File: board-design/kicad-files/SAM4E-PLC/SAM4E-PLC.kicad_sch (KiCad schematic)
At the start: 16 parts, among them U1 MCP7940N-xSN, U2 ATSAM4E16E

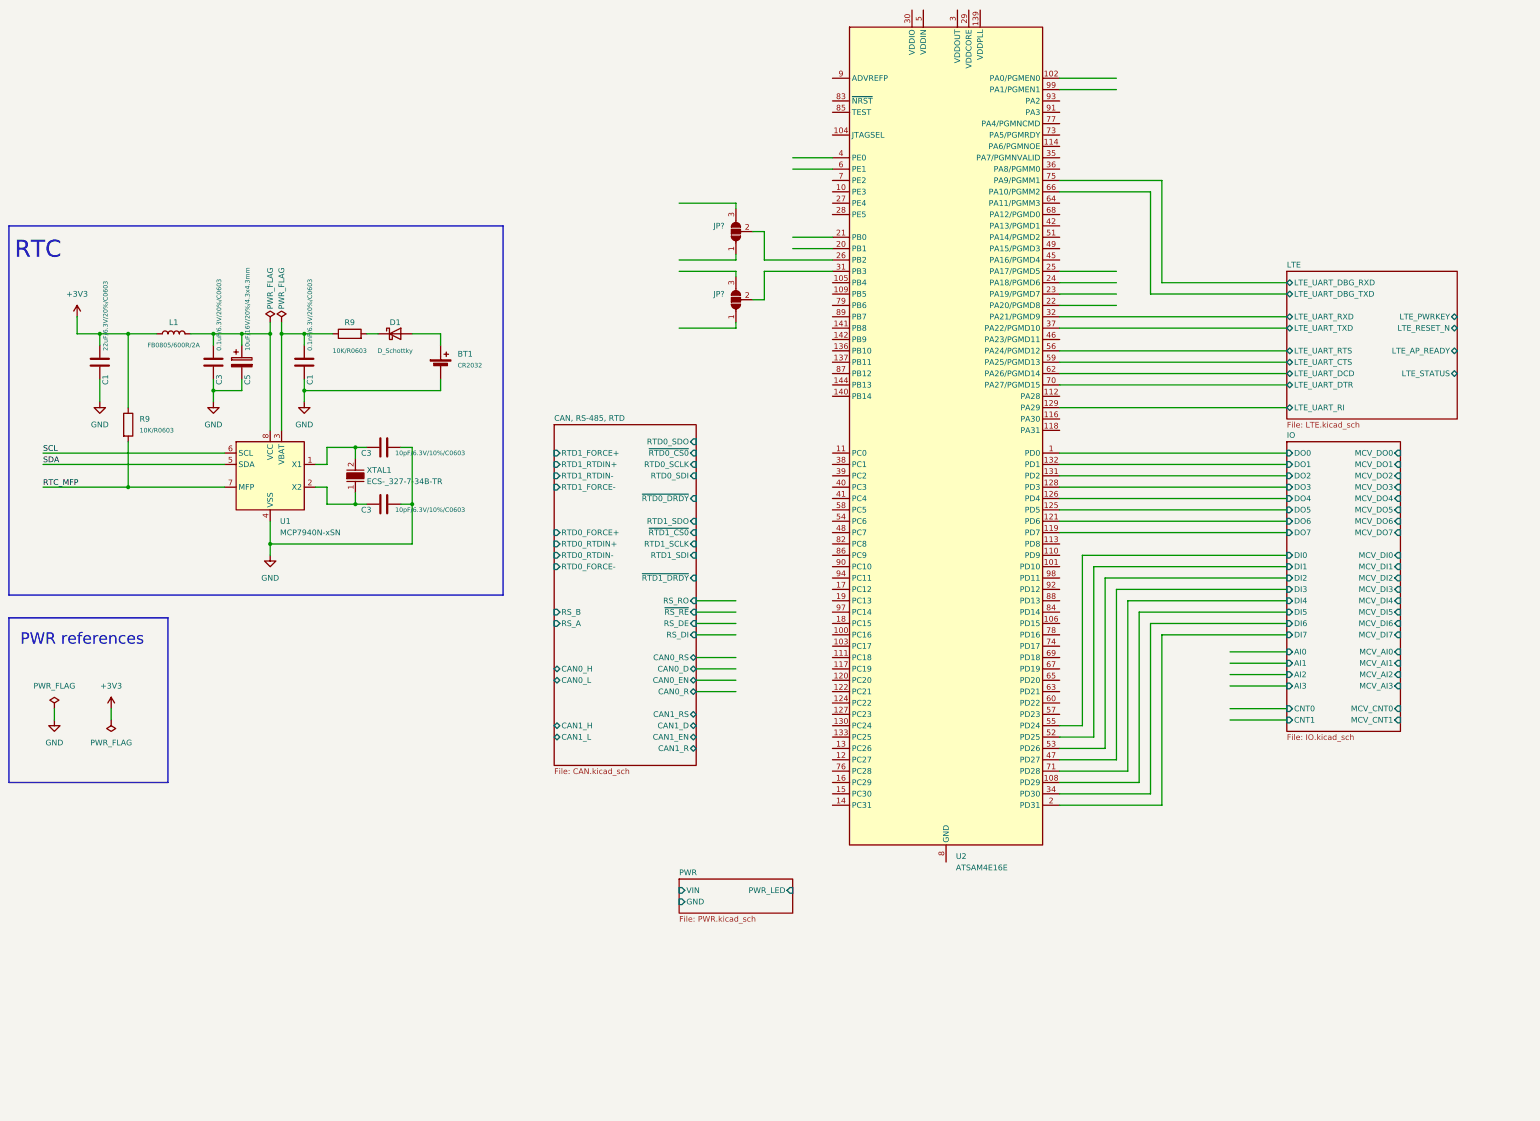
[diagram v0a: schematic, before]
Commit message: [FIX]
Updated footprints for tactile switches.

Signed-off-by: Nicolae-Andrei Vasile <vasilenicolaeandrei@gmail.com>
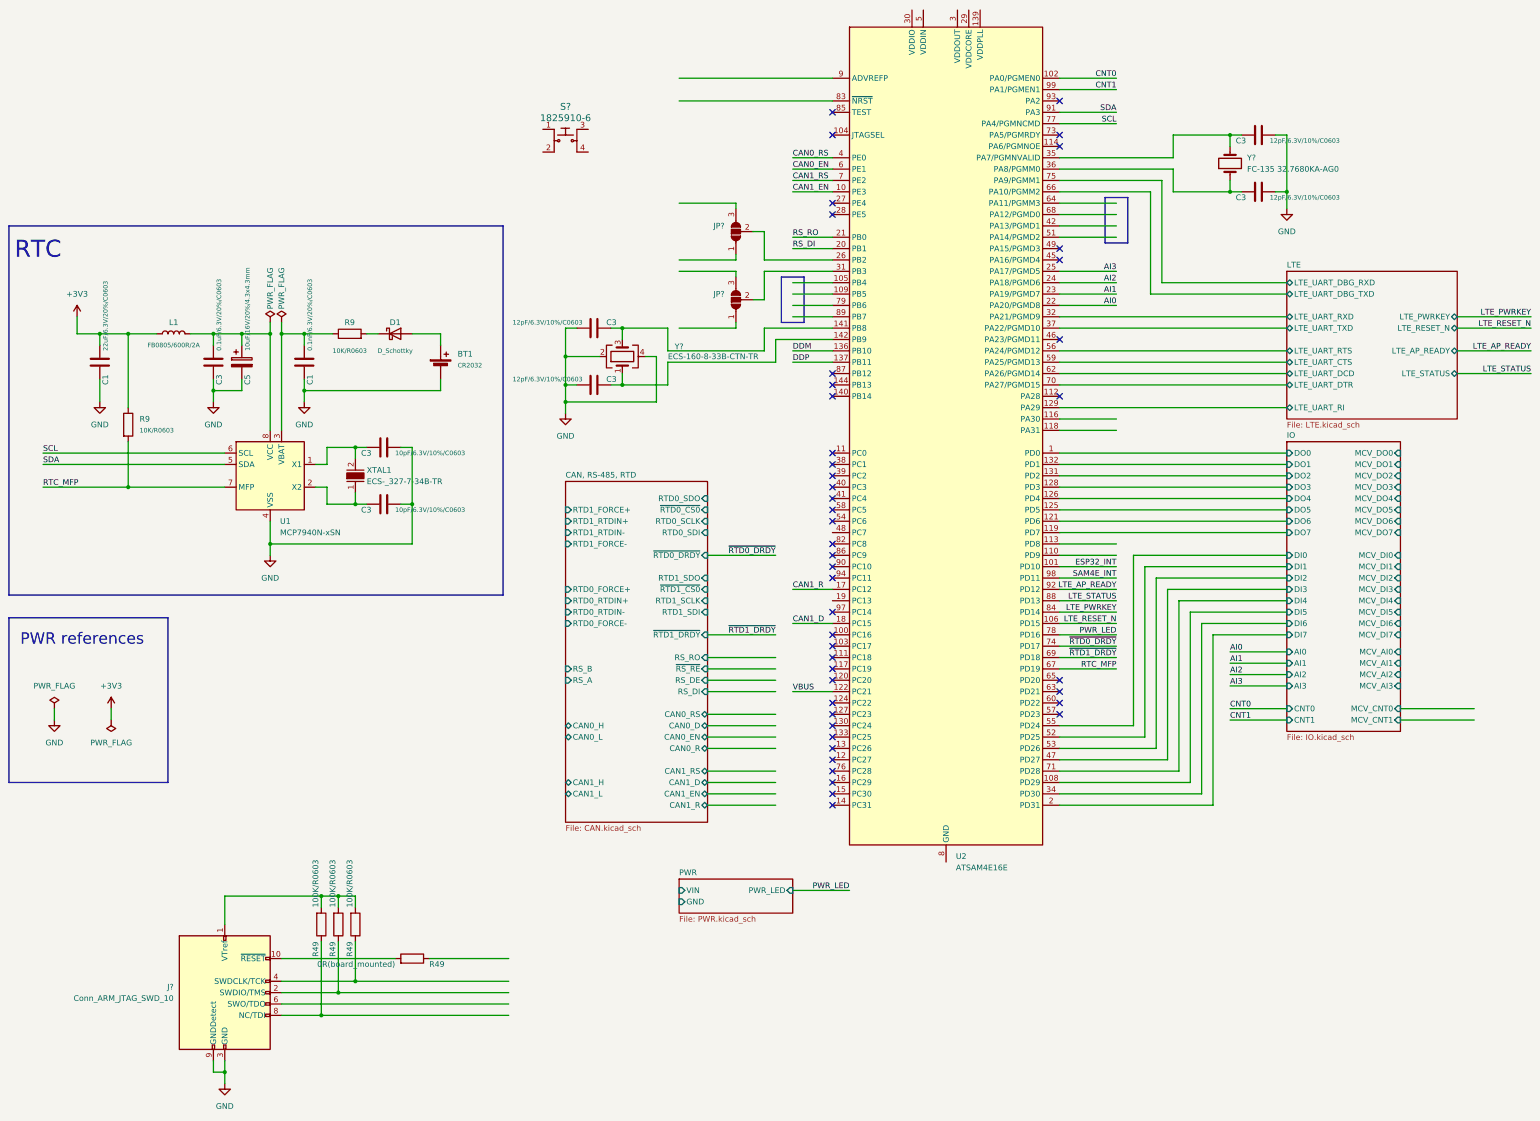
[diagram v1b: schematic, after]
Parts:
- added C3 (x4): 12pF/6.3V/10%/C0603, symbol Device:C
- added J?: Conn_ARM_JTAG_SWD_10, Connector_PinHeader_2.54mm:PinHeader_2x05_P2.54mm_Vertical, symbol Connector:Conn_ARM_JTAG_SWD_10
- added R49: 0R(board_mounted), Resistor_SMD:R_0402_1005Metric, symbol Device:R
- added R49 (x3): 100K/R0603, Resistor_SMD:R_0603_1608Metric, symbol Device:R
- added S?: 1825910-6, digikey-footprints:Switch_Tactile_THT_6x6mm, symbol dk_Tactile-Switches:1825910-6
- added Y?: FC-135 32.7680KA-AG0, Crystal:Crystal_SMD_3215-2Pin_3.2x1.5mm, symbol Device:Crystal
- added Y?: ECS-160-8-33B-CTN-TR, Crystal:Crystal_SMD_3225-4Pin_3.2x2.5mm, symbol Device:Crystal_GND24
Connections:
- net GND: now also C3.1, C3.1, C3.1, C3.1, J?.3 (GND), J?.5 (GND), J?.9 (GNDDetect), Y?.2, Y?.4
- net RTC_MFP: now also U2.67 (PD19)
- net SCL: now also U2.77 (PA4/PGMNCMD)
- net SDA: now also U2.91 (PA3)
- net CAN1_EN: now reaches U2.10 (PE3)
- net ESP32_INT: now reaches U2.101 (PD10)
- net CNT0: now reaches U2.102 (PA0/PGMEN0)
- net LTE_RESET_N: now reaches U2.106 (PD15)
- net VBUS: now reaches U2.122 (PC21)
- net DDM: now reaches U2.136 (PB10)
- net DDP: now reaches U2.137 (PB11)
- net at U2.141 (PB8): now also C3.2, Y?.3
- net at U2.142 (PB9): now also C3.2, Y?.1
- net CAN1_R: now reaches U2.17 (PC12)
- net CAN1_D: now reaches U2.18 (PC15)
- net RS_DI: now reaches U2.20 (PB1)
- net RS_RO: now reaches U2.21 (PB0)
- net AI0: now reaches U2.22 (PA20/PGMD8)
- net AI1: now reaches U2.23 (PA19/PGMD7)
- net AI2: now reaches U2.24 (PA18/PGMD6)
- net AI3: now reaches U2.25 (PA17/PGMD5)
- net at U2.35 (PA7/PGMNVALID): now also C3.2, Y?.2
- net at U2.36 (PA8/PGMM0): now also C3.2, Y?.1
- net CAN0_RS: now reaches U2.4 (PE0)
- net CAN0_EN: now reaches U2.6 (PE1)
- net ~{RTD1_DRDY}: now reaches U2.69 (PD18)
- net CAN1_RS: now reaches U2.7 (PE2)
- net ~{RTD0_DRDY}: now reaches U2.74 (PD17)
- net PWR_LED: now reaches U2.78 (PD16)
- net LTE_PWRKEY: now reaches U2.84 (PD14)
- net LTE_STATUS: now reaches U2.88 (PD13)
- net LTE_AP_READY: now reaches U2.92 (PD12)
- net SAM4E_INT: now reaches U2.98 (PD11)
- net CNT1: now reaches U2.99 (PA1/PGMEN1)
- new net: J?.10 (~{RESET}), R49.2
- new net: J?.2 (SWDIO/TMS), R49.1
- new net: J?.1 (VTref), R49.2, R49.2, R49.2
- new net: J?.4 (SWDCLK/TCK), R49.1
- new net: J?.8 (NC/TDI), R49.1
- no-connect marks 0 -> 45

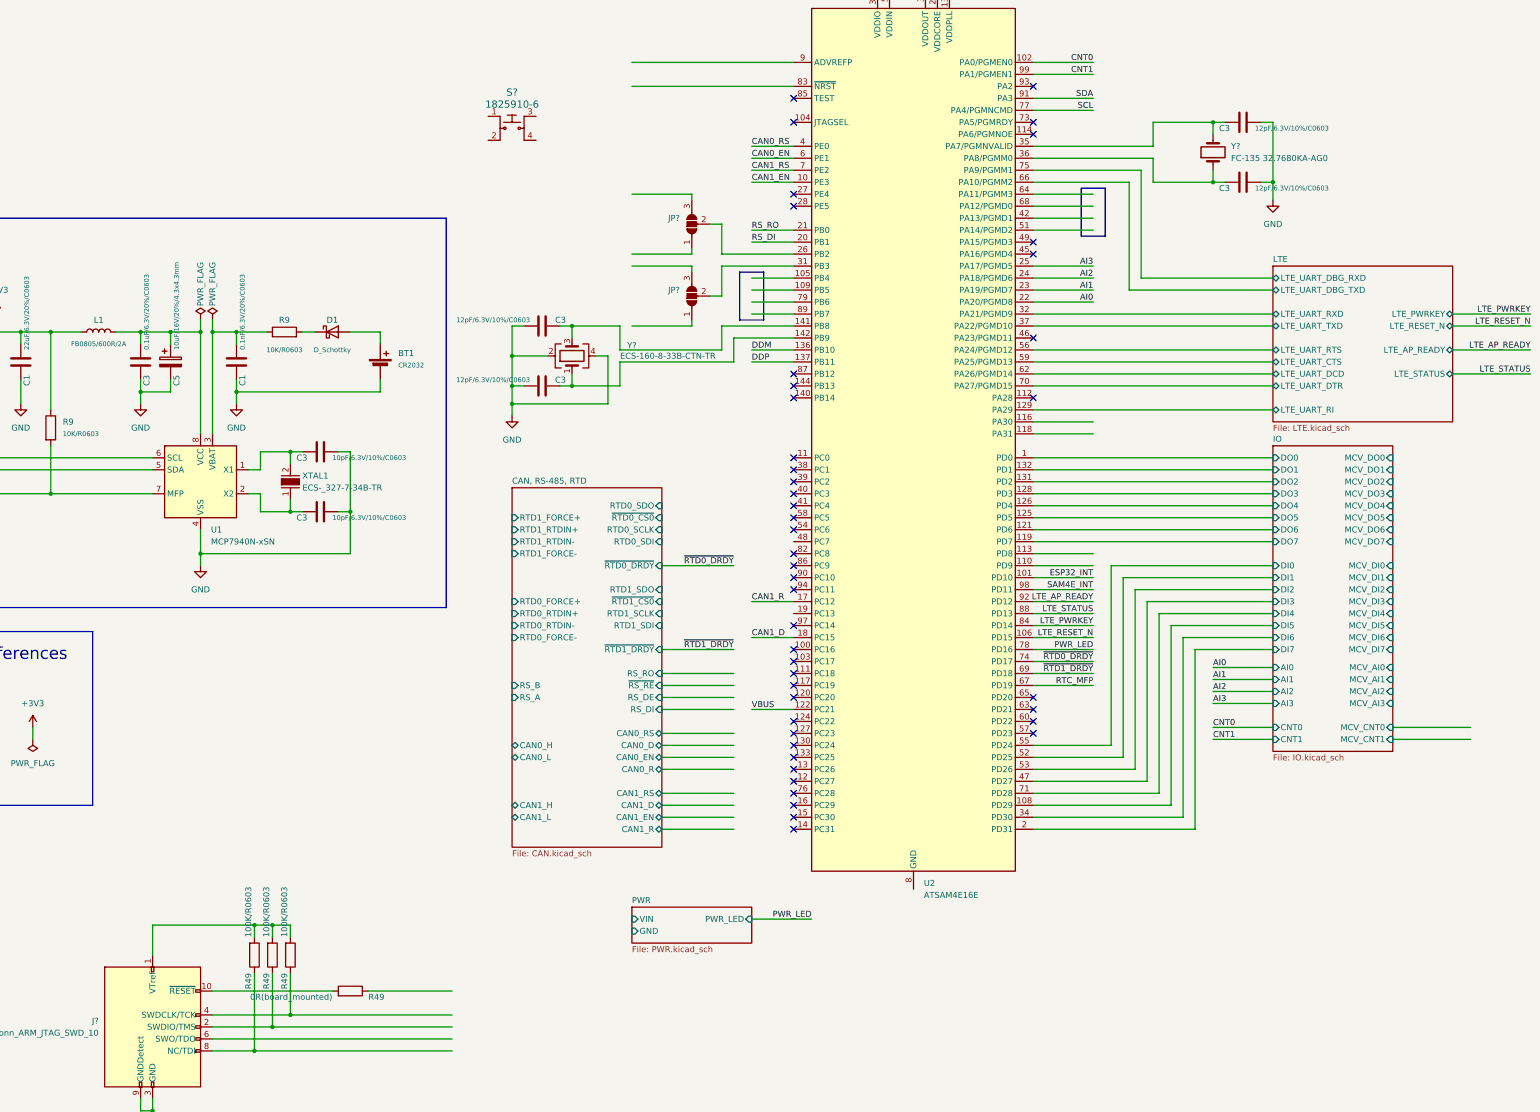
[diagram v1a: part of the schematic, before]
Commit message: [UPDATE]
Refactored schematic for LTE, Power and other schematic sub-sheets.

Signed-off-by: Nicolae-Andrei Vasile <vasilenicolaeandrei@gmail.com>
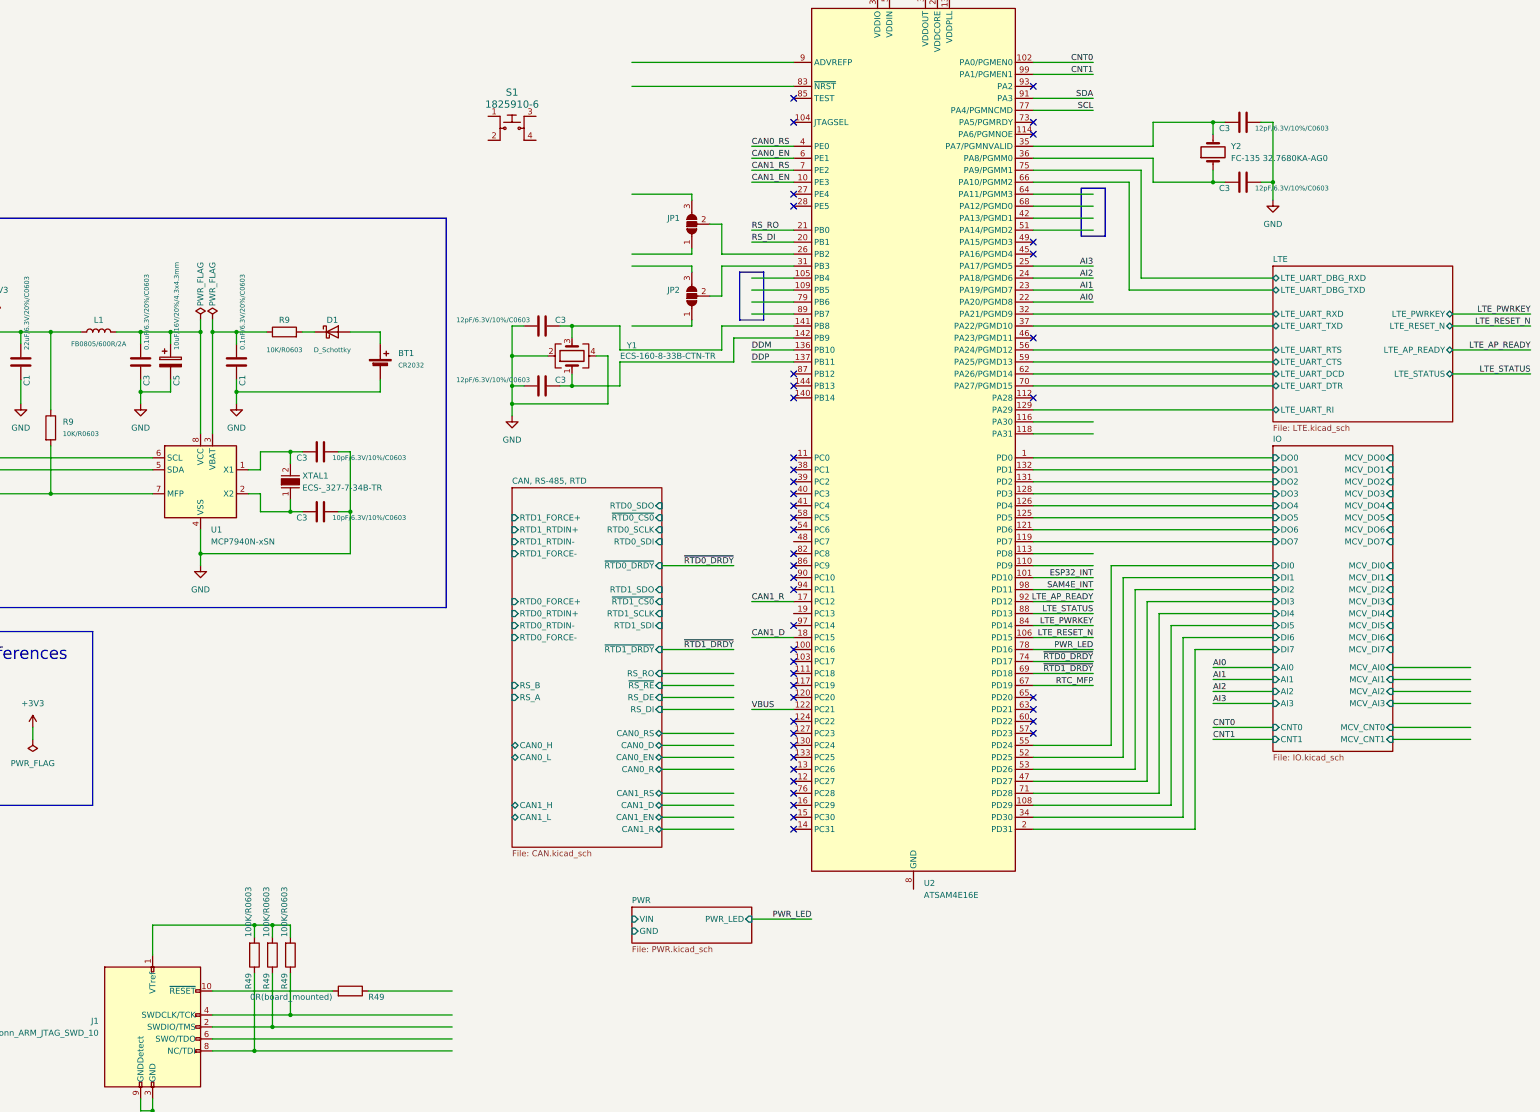
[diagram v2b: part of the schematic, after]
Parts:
- gave numbers to parts that had none: 6
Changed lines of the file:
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@@
+    (stroke (width 0) (type default))
+  )
+  (wire (pts (xy 326.39 170.18) (xy 342.9 170.18))
     (stroke (width 0) (type default))
   )
@@
     (stroke (width 0) (type default))
   )
+  (wire (pts (xy 326.39 165.1) (xy 342.9 165.1))
+    (stroke (width 0) (type default))
+  )
   (wire (pts (xy 190.5 218.44) (xy 203.2 218.44))
     (stroke (width 0) (type default))
@@
     (stroke (width 0) (type default))
   )
+  (wire (pts (xy 326.39 172.72) (xy 342.9 172.72))
+    (stroke (width 0) (type default))
+  )
   (wire (pts (xy 177.8 81.28) (xy 177.8 80.01))
     (stroke (width 0) (type default))
@@
   )
   (wire (pts (xy 190.5 72.39) (xy 199.39 72.39))
+    (stroke (width 0) (type default))
+  )
+  (wire (pts (xy 326.39 167.64) (xy 342.9 167.64))
     (stroke (width 0) (type default))
   )
@@
         )
         (path "/93076d8a-73da-4f5d-b7f2-28678f1db77d"
-          (reference "R?") (unit 1)
+          (reference "R6") (unit 1)
         )
       )
@@
   (symbol (lib_id "Device:Crystal") (at 288.29 55.88 90) (unit 1)
     (in_bom yes) (on_board yes) (dnp no) (fields_autoplaced)
-    (property "Reference" "Y?" (at 292.1 54.61 90)
+    (property "Reference" "Y2" (at 292.1 54.61 90)
       (effects (font (size 1.27 1.27)) (justify right))
     )
@@
       (project "SAM4E-PLC"
         (path "/93076d8a-73da-4f5d-b7f2-28678f1db77d"
-          (reference "Y?") (unit 1)
+          (reference "Y2") (unit 1)
         )
       )
@@
         )
         (path "/93076d8a-73da-4f5d-b7f2-28678f1db77d"
-          (reference "R?") (unit 1)
+          (reference "R3") (unit 1)
         )
       )
@@
         )
         (path "/93076d8a-73da-4f5d-b7f2-28678f1db77d"
-          (reference "C?") (unit 1)
+          (reference "C9") (unit 1)
         )
       )
@@
         )
         (path "/93076d8a-73da-4f5d-b7f2-28678f1db77d"
-          (reference "R?") (unit 1)
+          (reference "R5") (unit 1)
         )
       )
@@
   (symbol (lib_id "Jumper:SolderJumper_3_Open") (at 177.8 86.36 90) (unit 1)
     (in_bom yes) (on_board yes) (dnp no) (fields_autoplaced)
-    (property "Reference" "JP?" (at 175.26 85.09 90)
+    (property "Reference" "JP2" (at 175.26 85.09 90)
       (effects (font (size 1.27 1.27)) (justify left))
     )
@@
       (project "SAM4E-PLC"
         (path "/93076d8a-73da-4f5d-b7f2-28678f1db77d"
-          (reference "JP?") (unit 1)
+          (reference "JP2") (unit 1)
         )
       )
@@
         )
         (path "/93076d8a-73da-4f5d-b7f2-28678f1db77d"
-          (reference "#PWR07") (unit 1)
+          (reference "#PWR08") (unit 1)
         )
       )
@@
   (symbol (lib_id "dk_Tactile-Switches:1825910-6") (at 139.7 50.8 0) (unit 1)
     (in_bom yes) (on_board yes) (dnp no) (fields_autoplaced)
-    (property "Reference" "S?" (at 139.7 43.18 0)
+    (property "Reference" "S1" (at 139.7 43.18 0)
       (effects (font (size 1.524 1.524)))
     )
@@
       (project "SAM4E-PLC"
         (path "/93076d8a-73da-4f5d-b7f2-28678f1db77d"
-          (reference "S?") (unit 1)
+          (reference "S1") (unit 1)
         )
       )
@@
         )
         (path "/93076d8a-73da-4f5d-b7f2-28678f1db77d"
-          (reference "R2") (unit 1)
+          (reference "R4") (unit 1)
         )
       )
@@
   (symbol (lib_id "Connector:Conn_ARM_JTAG_SWD_10") (at 63.5 241.3 0) (unit 1)
     (in_bom yes) (on_board yes) (dnp no) (fields_autoplaced)
-    (property "Reference" "J?" (at 52.07 240.03 0)
+    (property "Reference" "J1" (at 52.07 240.03 0)
       (effects (font (size 1.27 1.27)) (justify right))
     )
@@
       (project "SAM4E-PLC"
         (path "/93076d8a-73da-4f5d-b7f2-28678f1db77d"
-          (reference "J?") (unit 1)
+          (reference "J1") (unit 1)
         )
       )
@@
         )
         (path "/93076d8a-73da-4f5d-b7f2-28678f1db77d"
-          (reference "C?") (unit 1)
+          (reference "C7") (unit 1)
         )
       )
@@
         )
         (path "/93076d8a-73da-4f5d-b7f2-28678f1db77d"
-          (reference "#PWR072") (unit 1)
+          (reference "#PWR09") (unit 1)
         )
       )
@@
         )
         (path "/93076d8a-73da-4f5d-b7f2-28678f1db77d"
-          (reference "#PWR06") (unit 1)
+          (reference "#PWR07") (unit 1)
         )
       )
@@
         )
         (path "/93076d8a-73da-4f5d-b7f2-28678f1db77d"
-          (reference "C?") (unit 1)
+          (reference "C8") (unit 1)
         )
       )
@@
         )
         (path "/93076d8a-73da-4f5d-b7f2-28678f1db77d"
-          (reference "R?") (unit 1)
+          (reference "R2") (unit 1)
         )
       )
@@
         )
         (path "/93076d8a-73da-4f5d-b7f2-28678f1db77d"
-          (reference "#PWR073") (unit 1)
+          (reference "#PWR06") (unit 1)
         )
       )
@@
         )
         (path "/93076d8a-73da-4f5d-b7f2-28678f1db77d"
-          (reference "C?") (unit 1)
+          (reference "C10") (unit 1)
         )
       )
@@
         )
         (path "/93076d8a-73da-4f5d-b7f2-28678f1db77d"
-          (reference "#PWR071") (unit 1)
+          (reference "#PWR010") (unit 1)
         )
       )
@@
   (symbol (lib_id "Jumper:SolderJumper_3_Open") (at 177.8 71.12 90) (unit 1)
     (in_bom yes) (on_board yes) (dnp no) (fields_autoplaced)
-    (property "Reference" "JP?" (at 175.26 69.85 90)
+    (property "Reference" "JP1" (at 175.26 69.85 90)
       (effects (font (size 1.27 1.27)) (justify left))
     )
@@
       (project "SAM4E-PLC"
         (path "/93076d8a-73da-4f5d-b7f2-28678f1db77d"
-          (reference "JP?") (unit 1)
+          (reference "JP1") (unit 1)
         )
       )
@@
   (symbol (lib_id "Device:Crystal_GND24") (at 152.4 99.06 90) (unit 1)
     (in_bom yes) (on_board yes) (dnp no)
-    (property "Reference" "Y?" (at 165.1 96.8441 90)
+    (property "Reference" "Y1" (at 165.1 96.8441 90)
       (effects (font (size 1.27 1.27)))
     )
@@
       (project "SAM4E-PLC"
         (path "/93076d8a-73da-4f5d-b7f2-28678f1db77d"
-          (reference "Y?") (unit 1)
-        )
-      )
+          (reference "Y1") (unit 1)
+        )
+      )
